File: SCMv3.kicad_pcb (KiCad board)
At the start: 0 parts

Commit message: SCHEM + PCB 6/
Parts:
- added BFAST1: ORANGE-LATCH, 4ms_Switch:Button_LED_PB61303, B.Cu at (7.80, 93.1)
- added BMUTE1: ORANGE-LATCH, 4ms_Switch:Button_LED_PB61303, B.Cu at (7.80, 105.0)
- added J1-OUT8: OUTPUT, 4ms_Jack:EighthInch_PJ398SM, B.Cu at (51.3, 104.6)
- added J2-OUT7: OUTPUT, 4ms_Jack:EighthInch_PJ398SM, B.Cu at (51.3, 92.3)
- added J3-OUT6: OUTPUT, 4ms_Jack:EighthInch_PJ398SM, B.Cu at (51.3, 79.9)
- added J4-OUT5: OUTPUT, 4ms_Jack:EighthInch_PJ398SM, B.Cu at (51.3, 67.5)
- added J5-OUT4: OUTPUT, 4ms_Jack:EighthInch_PJ398SM, B.Cu at (51.3, 55.1)
- added J6-OUT3: OUTPUT, 4ms_Jack:EighthInch_PJ398SM, B.Cu at (51.3, 42.7)
- added J7-OUT2: OUTPUT, 4ms_Jack:EighthInch_PJ398SM, B.Cu at (51.3, 30.4)
- added J8-OUT1: OUTPUT, 4ms_Jack:EighthInch_PJ398SM, B.Cu at (51.3, 18.0)
- added J9-CLK_IN: OUTPUT, 4ms_Jack:EighthInch_PJ398SM, B.Cu at (51.3, 5.59)
- added JFAST1: PJ301M-12, 4ms_Jack:EighthInch_PJ398SM, B.Cu at (31.3, 85.2)
- added JMUTE1: PJ301M-12, 4ms_Jack:EighthInch_PJ398SM, B.Cu at (31.3, 97.9)
- added JPW1: PJ301M-12, 4ms_Jack:EighthInch_PJ398SM, B.Cu at (31.3, 72.5)
- added JRESYNC1: PJ301M-12, 4ms_Jack:EighthInch_PJ398SM, B.Cu at (31.3, 9.03)
- added JROTATE1: PJ301M-12, 4ms_Jack:EighthInch_PJ398SM, B.Cu at (31.3, 21.7)
- added JSHUFFLE1: PJ301M-12, 4ms_Jack:EighthInch_PJ398SM, B.Cu at (31.3, 47.1)
- added JSKIP1: PJ301M-12, 4ms_Jack:EighthInch_PJ398SM, B.Cu at (31.3, 59.8)
- added JSLIP1: PJ301M-12, 4ms_Jack:EighthInch_PJ398SM, B.Cu at (31.3, 34.4)
- added LED1: BLUE, 4ms_LED:LED_PLCC-4, B.Cu at (42.1, 104.6)
- added LED2: GREEN, 4ms_LED:LED_PLCC-4, B.Cu at (42.1, 92.3)
- added LED3: GREEN, 4ms_LED:LED_PLCC-4, B.Cu at (42.1, 79.9)
- added LED4: GREEN, 4ms_LED:LED_PLCC-4, B.Cu at (42.1, 67.5)
- added LED5: GREEN, 4ms_LED:LED_PLCC-4, B.Cu at (42.1, 55.1)
- added LED6: GREEN, 4ms_LED:LED_PLCC-4, B.Cu at (42.1, 42.7)
- added LED7: BLUE, 4ms_LED:LED_PLCC-4, B.Cu at (42.1, 30.4)
- added LED8: BLUE, 4ms_LED:LED_PLCC-4, B.Cu at (42.1, 18.0)
- added LED9: WHITE, 4ms_LED:LED_PLCC-4, B.Cu at (42.1, 5.59)
- added PPW1: 10k Center Det, 4ms_Potentiometer:Pot_9mm_Dshaft_Det, B.Cu at (7.80, 79.6)
- added PROTATE1: 10k No Det, 4ms_Potentiometer:Pot_9mm_Dshaft_Det, B.Cu at (7.80, 9.03)
- added PSHUFFLE1: 10k No Det, 4ms_Potentiometer:Pot_9mm_Dshaft_Det, B.Cu at (7.80, 44.3)
- added PSKIP1: 10k No Det, 4ms_Potentiometer:Pot_9mm_Dshaft_Det, B.Cu at (7.80, 62.0)
- added PSLIP1: 10k Center Det, 4ms_Potentiometer:Pot_9mm_Dshaft_Det, B.Cu at (7.80, 26.7)
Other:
- board outline added: 58.7 x 110.9 mm
- copper layers 0 -> 16

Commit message: PCB + SCHEM 6/30
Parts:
- added C1: 330pF_0603_35V, 4ms_Capacitor:C_0603, F.Cu at (15.5, 44.5)
- added C10: 1nF_0603_50V, 4ms_Capacitor:C_0603, F.Cu at (10.3, 59.0)
- added C11: 1nF_0603_50V, 4ms_Capacitor:C_0603, F.Cu at (10.5, 76.9)
- added C12: 47uF_5x5.3_16V, 4ms_Capacitor:CP_Elec_5x5.3, F.Cu at (28.9, 42.5)
- added C13: 47uF_5x5.3_16V, 4ms_Capacitor:CP_Elec_5x5.3, F.Cu at (26.5, 28.5)
- added C14: 47uF_5x5.3_16V, 4ms_Capacitor:CP_Elec_5x5.3, F.Cu at (10.9, 31.7)
- added C15: 0.1uF_0603_16V, 4ms_Capacitor:C_0603, F.Cu at (14.2, 36.3)
- added C16: 0.1uF_0603_16V, 4ms_Capacitor:C_0603, F.Cu at (22.6, 20.3)
- added C2: 1nF_0603_50V, 4ms_Capacitor:C_0603, F.Cu at (15.5, 85.1)
- added C3: 330pF_0603_35V, 4ms_Capacitor:C_0603, F.Cu at (11.1, 6.06)
- added C4: 9pF_0603_50V, 4ms_Capacitor:C_0603, F.Cu at (13.9, 58.6)
- added C5: 9pF_0603_50V, 4ms_Capacitor:C_0603, F.Cu at (8.89, 47.6)
- added C6: 330pF_0603_35V, 4ms_Capacitor:C_0603, F.Cu at (10.6, 23.5)
- added C7: 1nF_0603_50V, 4ms_Capacitor:C_0603, F.Cu at (18.3, 100.5)
- added C8: 1nF_0603_50V, 4ms_Capacitor:C_0603, F.Cu at (10.5, 41.4)
- added C9: 1nF_0603_50V, 4ms_Capacitor:C_0603, F.Cu at (13.8, 41.2)
- added D1: BAT54S, 4ms_Package_SOT:SOT23-3_PO132, F.Cu at (10.8, 51.2)
- added D10: B140-E3, 4ms_Diode:D_SMA, F.Cu at (24.9, 12.8)
- added D11: B140-E3, 4ms_Diode:D_SMA, F.Cu at (18.0, 23.9)
- added D2: BAT54S, 4ms_Package_SOT:SOT23-3_PO132, F.Cu at (17.2, 87.8)
- added D3: BAT54S, 4ms_Package_SOT:SOT23-3_PO132, F.Cu at (7.81, 9.12)
- added D4: BAT54S, 4ms_Package_SOT:SOT23-3_PO132, F.Cu at (7.80, 26.5)
- added D5: BAT54S, 4ms_Package_SOT:SOT23-3_PO132, F.Cu at (18.2, 97.3)
- added D6: BAT54S, 4ms_Package_SOT:SOT23-3_PO132, F.Cu at (7.85, 43.9)
- added D7: BAT54S, 4ms_Package_SOT:SOT23-3_PO132, F.Cu at (17.1, 39.6)
- added D8: BAT54S, 4ms_Package_SOT:SOT23-3_PO132, F.Cu at (7.78, 61.6)
- added D9: BAT54S, 4ms_Package_SOT:SOT23-3_PO132, F.Cu at (7.84, 79.3)
- added IC1: 40106, 4ms_Package_SSOP:TSSOP-14_4.4x5mm_P0.65mm, F.Cu at (15.4, 67.5)
- added IC2: 40106, 4ms_Package_SSOP:TSSOP-14_4.4x5mm_P0.65mm, F.Cu at (23.3, 66.3)
- added IC3: TL082, 4ms_Package_SSOP:TSSOP-8_4.4x3mm_Pitch0.65mm, F.Cu at (32.6, 5.97)
- added J1: ISP, 4ms_Connector:Pins_2x03_2.54mm_TH, F.Cu at (20.3, 78.3)
- added J2: Conn_01x02, 4ms_Connector:Pins_1x02_2.54mm_TH, F.Cu at (26.3, 2.42)
- added J3: POWER, 4ms_Connector:Pins_2x08_2.54mm_TH, F.Cu at (18.0, 11.1)
- added Q1: Si2318, Package_TO_SOT_SMD:SOT-23, F.Cu at (3.47, 99.0)
- added Q2: Si2318, Package_TO_SOT_SMD:SOT-23, F.Cu at (32.1, 92.1)
- added Q3: Si2318, Package_TO_SOT_SMD:SOT-23, F.Cu at (14.1, 100.6)
- added Q4: Si2318, Package_TO_SOT_SMD:SOT-23, F.Cu at (32.8, 105.3)
- added R1: 4.7k_0603, 4ms_Resistor:R_0603, F.Cu at (39.5, 4.85)
- added R10: 470R_0805_350mW, 4ms_Resistor:R_0603, F.Cu at (7.78, 5.08)
- added R11: 100k_0603, 4ms_Resistor:R_0603, F.Cu at (35.6, 88.5)
- added R12: 1k_0603, 4ms_Resistor:R_0603, F.Cu at (46.1, 35.0)
- added R13: 470R_0805_350mW, 4ms_Resistor:R_0603, F.Cu at (15.9, 93.1)
- added R14: 4.7k_0603, 4ms_Resistor:R_0603, F.Cu at (42.9, 34.5)
- added R15: 1k_0603, 4ms_Resistor:R_0603, F.Cu at (46.1, 47.0)
- added R16: 10k_0603, 4ms_Resistor:R_0603, F.Cu at (18.1, 44.5)
- added R17: 4.7k_0603, 4ms_Resistor:R_0603, F.Cu at (42.0, 39.3)
- added R18: 100k_0603, 4ms_Resistor:R_0603, F.Cu at (9.39, 104.8)
- added R19: 1k_0603, 4ms_Resistor:R_0603, F.Cu at (46.1, 59.7)
- added R2: 4.7k_0603, 4ms_Resistor:R_0603, F.Cu at (42.1, 2.14)
- added R20: 4.7k_0603, 4ms_Resistor:R_0603, F.Cu at (42.0, 51.7)
- added R21: 470R_0805_350mW, 4ms_Resistor:R_0603, F.Cu at (7.87, 23.0)
- added R22: 470R_0805_350mW, 4ms_Resistor:R_0603, F.Cu at (8.70, 100.1)
- added R23: 1k_0603, 4ms_Resistor:R_0603, F.Cu at (46.1, 71.9)
- added R24: 10k_0603, 4ms_Resistor:R_0603, F.Cu at (36.2, 106.4)
- added R25: 4.7k_0603, 4ms_Resistor:R_0603, F.Cu at (42.1, 64.0)
- added R26: 100k_0603, 4ms_Resistor:R_0603, F.Cu at (35.7, 101.4)
- added R27: 470R_0805_350mW, 4ms_Resistor:R_0603, F.Cu at (16.2, 104.9)
- added R28: 1k_0603, 4ms_Resistor:R_0603, F.Cu at (46.2, 84.2)
- added R29: 4.7k_0603, 4ms_Resistor:R_0603, F.Cu at (42.1, 76.4)
- added R3: 470R_0805_350mW, 4ms_Resistor:R_0603, F.Cu at (46.0, 9.84)
- added R30: 100k_0603, 4ms_Resistor:R_0603, F.Cu at (35.5, 50.0)
- added R31: 1k_0603, 4ms_Resistor:R_0603, F.Cu at (46.1, 96.5)
- added R32: 4.7k_0603, 4ms_Resistor:R_0603, F.Cu at (42.0, 88.8)
- added R33: 100k_0603, 4ms_Resistor:R_0603, F.Cu at (7.87, 40.5)
- added R34: 1k_0603, 4ms_Resistor:R_0603, F.Cu at (46.1, 107.8)
- added R35: 4.7k_0603, 4ms_Resistor:R_0603, F.Cu at (42.0, 108.6)
- added R36: 470R_0805_350mW, 4ms_Resistor:R_0603, F.Cu at (38.6, 11.5)
- added R37: 100k_0603, 4ms_Resistor:R_0603, F.Cu at (35.3, 62.1)
- added R38: 100k_0603, 4ms_Resistor:R_0603, F.Cu at (7.79, 58.3)
- added R39: 100k_0603, 4ms_Resistor:R_0603, F.Cu at (35.6, 74.8)
- added R4: 4.7k_0603, 4ms_Resistor:R_0603, F.Cu at (42.8, 9.83)
- added R40: 470k_0603, 4ms_Resistor:R_0603, F.Cu at (26.4, 4.90)
- added R41: 100k_0603, 4ms_Resistor:R_0603, F.Cu at (7.84, 75.9)
- added R42: 10k_0603, 4ms_Resistor:R_0603, F.Cu at (28.3, 16.6)
- added R5: 100k_0603, 4ms_Resistor:R_0603, F.Cu at (7.07, 92.9)
- added R6: 1k_0603, 4ms_Resistor:R_0603, F.Cu at (46.1, 22.4)
- added R7: 470R_0805_350mW, 4ms_Resistor:R_0603, F.Cu at (8.98, 87.7)
- added R8: 4.7k_0603, 4ms_Resistor:R_0603, F.Cu at (42.8, 22.2)
- added R9: 10k_0603, 4ms_Resistor:R_0603, F.Cu at (35.7, 93.5)
- added TRIM1: TrimPot_T73YEt_10k, 4ms_Potentiometer:Pot_Trim_7x6.6mm_T73YE, F.Cu at (32.8, 14.7)
- added U1: ATmega328-A, 4ms_Package_QFP:TQFP-32_7x7mm_P0.8mm, F.Cu at (18.4, 51.5)
- added VR1: L78M05CDT, 4ms_Package_TO:TO-252-2, F.Cu at (18.6, 32.0)
- added VR2: UA78L09, 4ms_Package_SOT:SOT89-3, F.Cu at (22.2, 40.3)
- added Y1: 16MHz_18pF_FA238, 4ms_Crystal:FA-238, F.Cu at (5.06, 49.0)
- BFAST1, BMUTE1: value ORANGE-LATCH -> Button_DPDT_Orange_Latching
- J1-OUT8, J2-OUT7, J3-OUT6, J4-OUT5, J5-OUT4, J6-OUT3, J7-OUT2, J8-OUT1: value OUTPUT -> JACK-MONO-SWB
- J9-CLK_IN1: renamed from J9-CLK_IN; value OUTPUT -> JCLK_IN
- JFAST1, JMUTE1: value PJ301M-12 -> 3.5mm_Stereo_SymSmall_0.05
- JPW1: value PJ301M-12 -> JPW
- JRESYNC1: value PJ301M-12 -> JRESYNC
- JROTATE1: value PJ301M-12 -> JROTATE
- JSHUFFLE1: value PJ301M-12 -> JSHUFFLE
- JSKIP1: value PJ301M-12 -> JSKIP
- JSLIP1: value PJ301M-12 -> JSLIP
- PPW1, PSLIP1: value 10k Center Det -> 9mm_CtrDet_10k_DShaft
- PROTATE1, PSHUFFLE1, PSKIP1: value 10k No Det -> 9mm_CtrDet_10k_DShaft
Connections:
- BFAST1 pad 1: Net-(BFAST1-Pad1) -> unconnected-(BFAST1-Pad1)
- BFAST1 pad 3: Net-(BFAST1-Pad3) -> unconnected-(BFAST1-Pad3)
- BFAST1 pad 4: Net-(BFAST1-Pad1) -> Net-(BFAST1-Pad4)
- BFAST1 pad 5: Net-(BFAST1-Pad2) -> Net-(BFAST1-Pad5)
- BFAST1 pad 6: Net-(BFAST1-Pad3) -> Net-(BFAST1-Pad6)
- BMUTE1 pad 1: Net-(BMUTE1-Pad1) -> unconnected-(BMUTE1-Pad1)
- BMUTE1 pad 3: Net-(BMUTE1-Pad3) -> unconnected-(BMUTE1-Pad3)
- BMUTE1 pad 4: Net-(BMUTE1-Pad1) -> Net-(BMUTE1-Pad4)
- BMUTE1 pad 5: Net-(BMUTE1-Pad2) -> Net-(BMUTE1-Pad5)
- BMUTE1 pad 6: Net-(BMUTE1-Pad3) -> Net-(BMUTE1-Pad6)
- J1-OUT8 pad 2: AGND -> GND
- J1-OUT8 pad 3: Net-(H6-Pad3) -> unconnected-(J1-OUT8-Pad3)
- J2-OUT7 pad 2: AGND -> GND
- J2-OUT7 pad 3: Net-(J2-OUT1-Pad3) -> unconnected-(J2-OUT7-Pad3)
- J3-OUT6 pad 2: AGND -> GND
- J3-OUT6 pad 3: Net-(J3-OUT2-Pad3) -> unconnected-(J3-OUT6-Pad3)
- J4-OUT5 pad 2: AGND -> GND
- J4-OUT5 pad 3: Net-(J4-OUT3-Pad3) -> unconnected-(J4-OUT5-Pad3)
- J5-OUT4 pad 2: AGND -> GND
- J5-OUT4 pad 3: Net-(J5-OUT4-Pad3) -> unconnected-(J5-OUT4-Pad3)
- J6-OUT3 pad 2: AGND -> GND
- J6-OUT3 pad 3: Net-(J6-OUT5-Pad3) -> unconnected-(J6-OUT3-Pad3)
- J7-OUT2 pad 2: AGND -> GND
- J7-OUT2 pad 3: Net-(J7-OUT6-Pad3) -> unconnected-(J7-OUT2-Pad3)
- J8-OUT1 pad 2: AGND -> GND
- J8-OUT1 pad 3: Net-(J8-OUT7-Pad3) -> unconnected-(J8-OUT1-Pad3)
- J9-CLK_IN1 pad 2: AGND -> GND
- J9-CLK_IN1 pad 3: Net-(J9-OUT8-Pad3) -> /IN-SW
- JFAST1 pad 1: Net-(BFAST1-Pad1) -> Net-(BFAST1-Pad4)
- JMUTE1 pad 1: Net-(BMUTE1-Pad1) -> Net-(BMUTE1-Pad4)
- JPW1 pad 3: Net-(JPW1-Pad3) -> unconnected-(JPW1-Pad3)
- JSHUFFLE1 pad 3: Net-(JSHUFFLE1-Pad3) -> unconnected-(JSHUFFLE1-Pad3)
- JSKIP1 pad 3: Net-(JSKIP1-Pad3) -> unconnected-(JSKIP1-Pad3)
- LED1 pad 1: (no net) -> unconnected-(LED1-Pad1)
- LED1 pad 2: (no net) -> /VREF
- LED1 pad 3: (no net) -> Net-(LED1-Pad3)
- LED1 pad 4: (no net) -> unconnected-(LED1-Pad4)
- LED2 pad 1: (no net) -> unconnected-(LED2-Pad1)
- LED2 pad 2: (no net) -> /VREF
- LED2 pad 3: (no net) -> unconnected-(LED2-Pad3)
- LED2 pad 4: (no net) -> Net-(LED2-Pad4)
- LED3 pad 1: (no net) -> unconnected-(LED3-Pad1)
- LED3 pad 2: (no net) -> /VREF
- LED3 pad 3: (no net) -> unconnected-(LED3-Pad3)
- LED3 pad 4: (no net) -> Net-(LED3-Pad4)
- LED4 pad 1: (no net) -> unconnected-(LED4-Pad1)
- LED4 pad 2: (no net) -> /VREF
- LED4 pad 3: (no net) -> unconnected-(LED4-Pad3)
- LED4 pad 4: (no net) -> Net-(LED4-Pad4)
- LED5 pad 1: (no net) -> unconnected-(LED5-Pad1)
- LED5 pad 2: (no net) -> /VREF
- LED5 pad 3: (no net) -> unconnected-(LED5-Pad3)
- LED5 pad 4: (no net) -> Net-(LED5-Pad4)
- LED6 pad 1: (no net) -> unconnected-(LED6-Pad1)
- LED6 pad 2: (no net) -> /VREF
- LED6 pad 3: (no net) -> unconnected-(LED6-Pad3)
- LED6 pad 4: (no net) -> Net-(LED6-Pad4)
- LED7 pad 1: (no net) -> unconnected-(LED7-Pad1)
- LED7 pad 2: (no net) -> /VREF
- LED7 pad 3: (no net) -> Net-(LED7-Pad3)
- LED7 pad 4: (no net) -> unconnected-(LED7-Pad4)
- LED8 pad 1: (no net) -> unconnected-(LED8-Pad1)
- LED8 pad 2: (no net) -> /VREF
- LED8 pad 3: (no net) -> Net-(LED8-Pad3)
- LED8 pad 4: (no net) -> unconnected-(LED8-Pad4)
- LED9 pad 1: (no net) -> Net-(LED9-Pad1)
- LED9 pad 2: (no net) -> /VREF
- LED9 pad 3: (no net) -> Net-(LED9-Pad3)
- LED9 pad 4: (no net) -> Net-(LED9-Pad4)
- PPW1 pad 1: GND -> +5V
- PPW1 pad 3: +5V -> GND
- PPW1 pad 4: (no net) -> GND
- PPW1 pad 5: (no net) -> GND
- PROTATE1 pad 4: (no net) -> GND
- PROTATE1 pad 5: (no net) -> GND
- PSHUFFLE1 pad 1: GND -> +5V
- PSHUFFLE1 pad 3: +5V -> GND
- PSHUFFLE1 pad 4: (no net) -> GND
- PSHUFFLE1 pad 5: (no net) -> GND
- PSKIP1 pad 1: GND -> +5V
- PSKIP1 pad 3: +5V -> GND
- PSKIP1 pad 4: (no net) -> GND
- PSKIP1 pad 5: (no net) -> GND
- PSLIP1 pad 4: (no net) -> GND
- PSLIP1 pad 5: (no net) -> GND

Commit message: PCB +SCHEM 7/02
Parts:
- added C17: 0.1uF_0603_16V, 4ms_Capacitor:C_0603, F.Cu at (54.8, 64.3)
- added C18: 0.1uF_0603_16V, 4ms_Capacitor:C_0603, F.Cu at (46.4, 60.1)
- added C19: 0.1uF_0603_16V, 4ms_Capacitor:C_0603, F.Cu at (23.2, 42.3)
- added C20: 0.1uF_0603_16V, 4ms_Capacitor:C_0603, F.Cu at (27.9, 80.7)
- added C21: 0.1uF_0603_16V, 4ms_Capacitor:C_0603, F.Cu at (33.2, 52.2)
- moved IC1 35.1 mm to (50.1, 62.4), turned to -90 degrees
- moved C1 33.6 mm to (15.1, 78.0), turned to -90 degrees
- moved Y1 29.8 mm to (20.5, 74.5), turned to 90 degrees
- moved C5 28.3 mm to (17.7, 74.5), turned to -90 degrees
- moved D7 27.8 mm to (8.07, 66.0), turned to -90 degrees
- moved C9 25.9 mm to (10.8, 66.9)
- moved R16 25.7 mm to (12.7, 69.7), turned to -90 degrees
- moved C15 24.3 mm to (20.2, 59.8), turned to 180 degrees
- moved D1 23.6 mm to (14.1, 74.6), turned to -90 degrees
- moved C4 20.2 mm to (20.4, 77.7), turned to 180 degrees
- moved IC2 16.3 mm to (33.0, 79.5), turned to 180 degrees
- moved U1 15.2 mm to (19.2, 66.7), turned to 90 degrees
- moved R22 13.1 mm to (21.8, 100.3)
- moved Q1 12.2 mm to (15.4, 101.5)
- moved R5 11.8 mm to (18.1, 97.1), turned to 90 degrees
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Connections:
- net /-12V renamed Net-(D11-Pad1)
- net Net-(IC3-Pad4) renamed -12VA
- IC1 pad 7: GND -> Net-(C18-Pad1)
- IC2 pad 7: GND -> Net-(C21-Pad1)
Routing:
- net GND: track 0.00 -> 629.4 mm, vias 0 -> 40
- net +5V: track 0.00 -> 217.4 mm, vias 0 -> 18
- net +12V: track 0.00 -> 152.9 mm, vias 0 -> 11
- net /VREF: track 0.00 -> 115.0 mm, vias 0 -> 5
- net +9V: track 0.00 -> 109.6 mm, vias 0 -> 12
- net /UC_IN: track 0.00 -> 83.6 mm, vias 0 -> 3
- net /UC_CLK_IN: track 0.00 -> 81.0 mm, vias 0 -> 3
- net /UC_OUT4_MOSI: track 0.00 -> 77.6 mm, vias 0 -> 6
- net /UC_OUT1: track 0.00 -> 76.1 mm
- net /UC_OUT6_SCK: track 0.00 -> 74.1 mm, vias 0 -> 9
- net /UC_SYNC: track 0.00 -> 73.1 mm, vias 0 -> 5
- net /UC_OUT8: track 0.00 -> 63.8 mm, vias 0 -> 7
- net /UC_OUT2: track 0.00 -> 61.4 mm
- net /UC_PW: track 0.00 -> 61.1 mm, vias 0 -> 7
- net /UC_SHUFFLE: track 0.00 -> 60.2 mm, vias 0 -> 3
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
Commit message: SCM PCB+SCHEM 7/05
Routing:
- net GND: track 629.4 -> 699.2 mm, vias 40 -> 56
- net +5V: track 217.4 -> 223.5 mm, vias 18 -> 19
- net +12V: track 152.9 -> 147.7 mm
- net Net-(BFAST1-Pad6): track 26.7 -> 27.3 mm
- net +9V: track 109.6 -> 109.7 mm, vias 12 -> 11

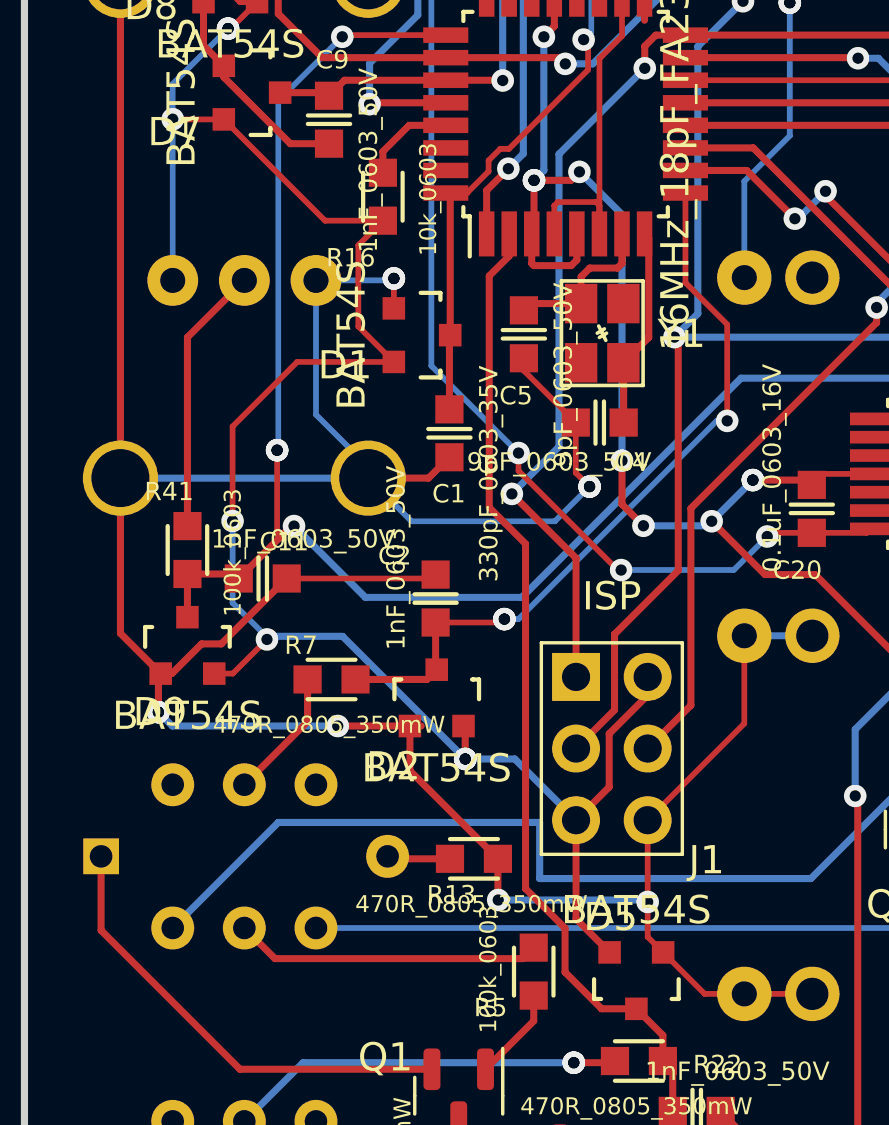
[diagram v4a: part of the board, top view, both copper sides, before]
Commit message: Fixes/tweaks to sch+pcb:
-Changed PCB form 16-layer to 2-layer board.
-RESET net was attached to +5V, moved it to _RESET/PC6 pin 29 of U1
-Renamed net UC_IN to UC_LED_IN (it only drives the IN LED, nothing else)
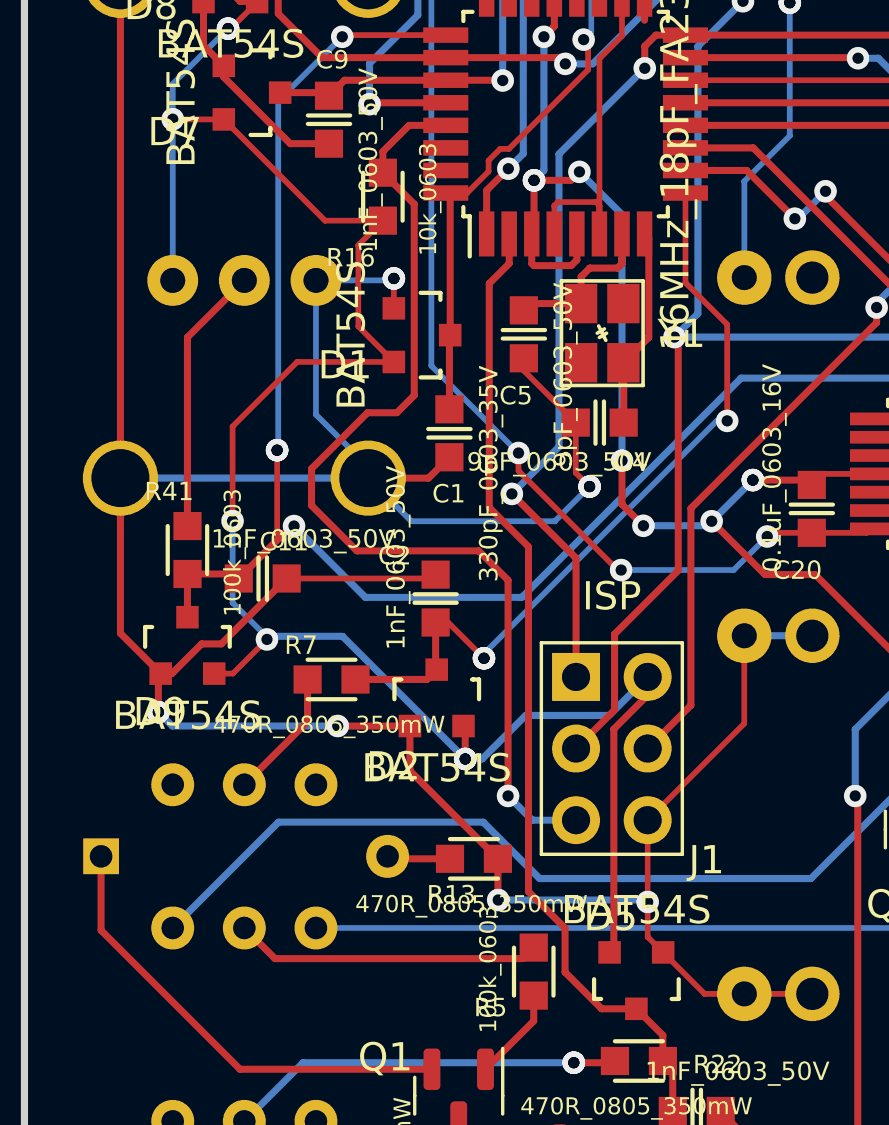
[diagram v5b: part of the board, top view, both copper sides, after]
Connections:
- net /UC_IN renamed /UC_LED_IN
- J1 pad 5: +5V -> /RESET
- R16 pad 1: Net-(R16-Pad1) -> /RESET
- U1 pad 29: Net-(R16-Pad1) -> /RESET
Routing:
- net /RESET: track 0.00 -> 36.4 mm, vias 0 -> 1
- net Net-(R16-Pad1): track 3.37 -> 0.00 mm
- net +5V: track 223.5 -> 225.1 mm
- net Net-(BFAST1-Pad4): track 41.6 -> 40.5 mm
- net /UC_FAST: track 26.9 -> 28.0 mm
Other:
- copper layers 16 -> 2
